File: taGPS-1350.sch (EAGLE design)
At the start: 84 parts, among them IC1 MSP430FR698X(1)80-PIN_PN, IC3 FT232RL

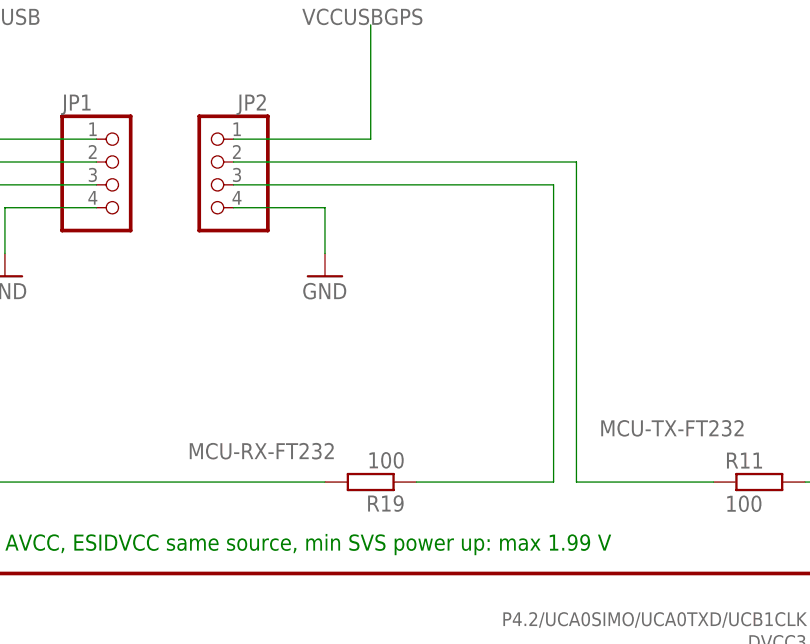
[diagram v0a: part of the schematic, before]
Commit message: Fix MCU RX/TX pinheader position, polish boards
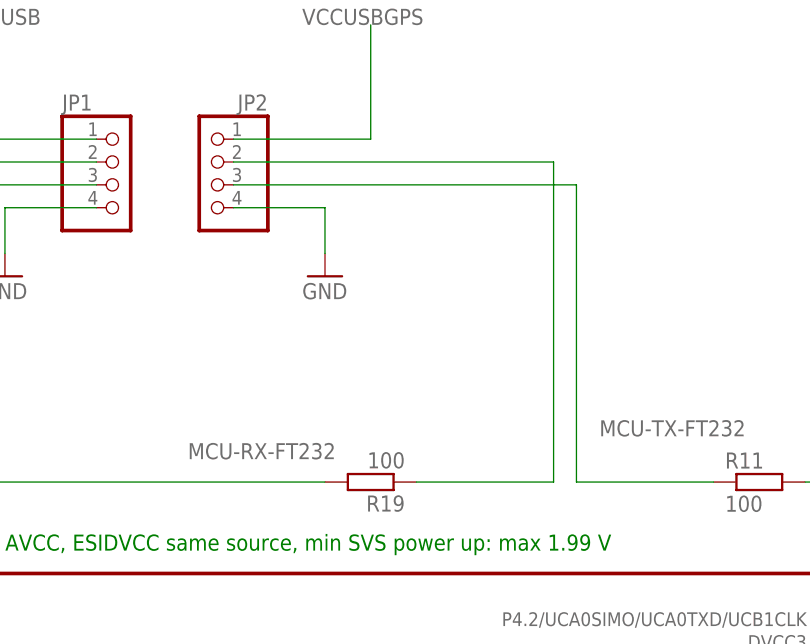
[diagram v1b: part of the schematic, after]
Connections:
- net MCU-TX-FT232: now also JP2.3; no longer JP2.2
- net N$8: now also JP2.2; no longer JP2.3
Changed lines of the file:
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@@
 <label x="-38.1" y="45.72" size="1.778" layer="95"/>
 <wire x1="-25.4" y1="40.64" x2="-40.64" y2="40.64" width="0.1524" layer="91"/>
-<wire x1="-40.64" y1="40.64" x2="-40.64" y2="76.2" width="0.1524" layer="91"/>
-<pinref part="JP2" gate="A" pin="2"/>
-<wire x1="-40.64" y1="76.2" x2="-78.74" y2="76.2" width="0.1524" layer="91"/>
+<wire x1="-40.64" y1="40.64" x2="-40.64" y2="73.66" width="0.1524" layer="91"/>
+<pinref part="JP2" gate="A" pin="3"/>
+<wire x1="-78.74" y1="73.66" x2="-40.64" y2="73.66" width="0.1524" layer="91"/>
 </segment>
 </net>
@@
 <pinref part="R19" gate="G$1" pin="1"/>
 <wire x1="-58.42" y1="40.64" x2="-43.18" y2="40.64" width="0.1524" layer="91"/>
-<wire x1="-43.18" y1="40.64" x2="-43.18" y2="73.66" width="0.1524" layer="91"/>
-<pinref part="JP2" gate="A" pin="3"/>
-<wire x1="-43.18" y1="73.66" x2="-78.74" y2="73.66" width="0.1524" layer="91"/>
-</segment>
-</net>
+<wire x1="-43.18" y1="40.64" x2="-43.18" y2="76.2" width="0.1524" layer="91"/>
+<pinref part="JP2" gate="A" pin="2"/>
+<wire x1="-43.18" y1="76.2" x2="-78.74" y2="76.2" width="0.1524" layer="91"/>
+</segment>
+</net>

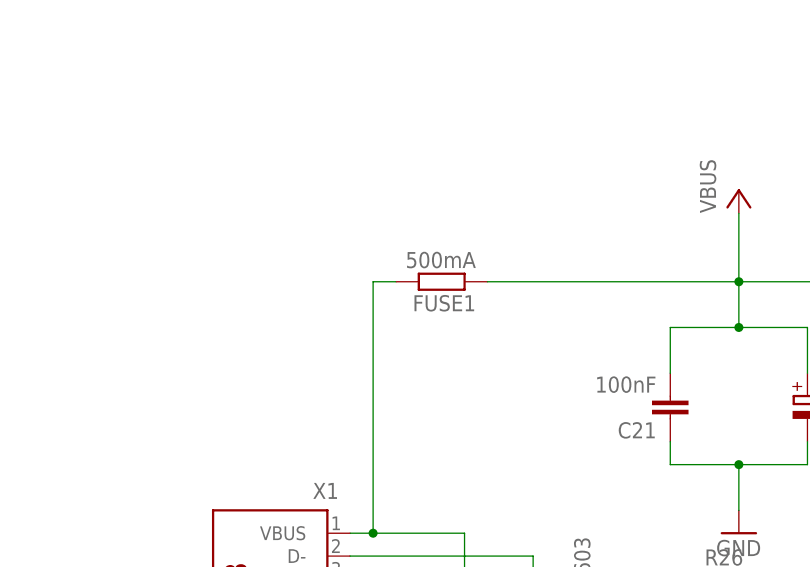
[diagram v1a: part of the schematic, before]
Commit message: Replace FUSE package to 1812
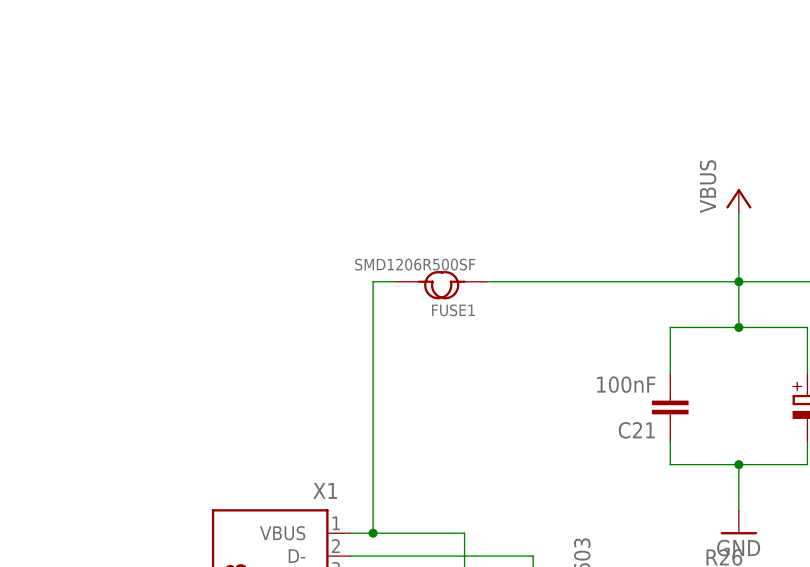
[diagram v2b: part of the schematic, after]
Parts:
- FUSE1: value 500mA -> SMD1206R500SF; device tagps:R-EU_R0805 -> tagps:SMD-PPTC-500MA-15V(1812)
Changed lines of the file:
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@@
 <layer number="48" name="Document" color="7" fill="1" visible="no" active="no"/>
 <layer number="49" name="Reference" color="7" fill="1" visible="no" active="no"/>
+<layer number="50" name="dxf" color="7" fill="1" visible="no" active="no"/>
 <layer number="51" name="tDocu" color="7" fill="1" visible="no" active="no"/>
 <layer number="52" name="bDocu" color="7" fill="1" visible="no" active="no"/>
+<layer number="53" name="tGND_GNDA" color="7" fill="9" visible="no" active="no"/>
+<layer number="54" name="bGND_GNDA" color="1" fill="9" visible="no" active="no"/>
+<layer number="56" name="wert" color="7" fill="1" visible="no" active="no"/>
+<layer number="57" name="tCAD" color="7" fill="1" visible="no" active="no"/>
 <layer number="90" name="Modules" color="5" fill="1" visible="yes" active="yes"/>
 <layer number="91" name="Nets" color="2" fill="1" visible="yes" active="yes"/>
@@
 <layer number="98" name="Guide" color="6" fill="1" visible="yes" active="yes"/>
 <layer number="99" name="SpiceOrder" color="5" fill="1" visible="yes" active="yes"/>
+<layer number="100" name="Muster" color="7" fill="1" visible="no" active="no"/>
+<layer number="101" name="Patch_Top" color="12" fill="4" visible="no" active="no"/>
+<layer number="102" name="Vscore" color="7" fill="1" visible="no" active="no"/>
+<layer number="103" name="tMap" color="7" fill="1" visible="no" active="no"/>
+<layer number="104" name="Name" color="7" fill="1" visible="no" active="no"/>
+<layer number="105" name="tPlate" color="7" fill="1" visible="no" active="no"/>
+<layer number="106" name="bPlate" color="7" fill="1" visible="no" active="no"/>
+<layer number="107" name="Crop" color="7" fill="1" visible="no" active="no"/>
+<layer number="108" name="fp8" color="7" fill="1" visible="yes" active="yes"/>
+<layer number="109" name="fp9" color="7" fill="1" visible="yes" active="yes"/>
+<layer number="110" name="110" color="7" fill="1" visible="yes" active="yes"/>
+<layer number="111" name="111" color="7" fill="1" visible="yes" active="yes"/>
+<layer number="112" name="tSilk" color="7" fill="1" visible="yes" active="yes"/>
+<layer number="113" name="IDFDebug" color="7" fill="1" visible="yes" active="yes"/>
+<layer number="114" name="FRNTMAAT1" color="7" fill="1" visible="no" active="no"/>
+<layer number="115" name="FRNTMAAT2" color="7" fill="1" visible="no" active="no"/>
+<layer number="116" name="Patch_BOT" color="9" fill="4" visible="no" active="no"/>
+<layer number="117" name="BACKMAAT1" color="7" fill="1" visible="no" active="no"/>
+<layer number="118" name="Rect_Pads" color="7" fill="1" visible="yes" active="yes"/>
+<layer number="119" name="KAP_TEKEN" color="7" fill="1" visible="no" active="no"/>
+<layer number="120" name="KAP_MAAT1" color="7" fill="1" visible="no" active="no"/>
+<layer number="121" name="_tsilk" color="7" fill="1" visible="no" active="no"/>
+<layer number="122" name="_bsilk" color="7" fill="1" visible="no" active="no"/>
+<layer number="123" name="tTestmark" color="7" fill="1" visible="yes" active="yes"/>
+<layer number="124" name="bTestmark" color="7" fill="1" visible="yes" active="yes"/>
+<layer number="125" name="_tNames" color="7" fill="1" visible="yes" active="yes"/>
+<layer number="126" name="_bNames" color="7" fill="1" visible="yes" active="yes"/>
+<layer number="127" name="_tValues" color="7" fill="1" visible="yes" active="yes"/>
+<layer number="128" name="_bValues" color="7" fill="1" visible="yes" active="yes"/>
+<layer number="130" name="SMDSTROOK" color="7" fill="1" visible="no" active="no"/>
+<layer number="131" name="tAdjust" color="7" fill="1" visible="yes" active="yes"/>
+<layer number="132" name="bAdjust" color="7" fill="1" visible="yes" active="yes"/>
+<layer number="144" name="DrillLegend" color="7" fill="1" visible="no" active="no"/>
+<layer number="150" name="Notes" color="7" fill="1" visible="yes" active="yes"/>
+<layer number="151" name="HeatSink" color="14" fill="1" visible="no" active="no"/>
+<layer number="152" name="_bDocu" color="7" fill="1" visible="yes" active="yes"/>
+<layer number="153" name="FabDoc1" color="6" fill="1" visible="no" active="no"/>
+<layer number="154" name="FabDoc2" color="2" fill="1" visible="no" active="no"/>
+<layer number="155" name="FabDoc3" color="7" fill="15" visible="no" active="no"/>
+<layer number="199" name="Contour" color="7" fill="1" visible="yes" active="yes"/>
+<layer number="200" name="200bmp" color="1" fill="10" visible="no" active="no"/>
+<layer number="201" name="201bmp" color="2" fill="1" visible="no" active="no"/>
+<layer number="202" name="202bmp" color="3" fill="1" visible="no" active="no"/>
+<layer number="203" name="203bmp" color="4" fill="10" visible="no" active="no"/>
+<layer number="204" name="204bmp" color="5" fill="10" visible="no" active="no"/>
+<layer number="205" name="205bmp" color="6" fill="10" visible="no" active="no"/>
+<layer number="206" name="206bmp" color="7" fill="10" visible="no" active="no"/>
+<layer number="207" name="207bmp" color="15" fill="10" visible="no" active="no"/>
+<layer number="208" name="208bmp" color="9" fill="10" visible="no" active="no"/>
+<layer number="209" name="209bmp" color="7" fill="1" visible="no" active="no"/>
+<layer number="210" name="210bmp" color="7" fill="1" visible="no" active="no"/>
+<layer number="211" name="211bmp" color="7" fill="1" visible="no" active="no"/>
+<layer number="212" name="212bmp" color="7" fill="1" visible="no" active="no"/>
+<layer number="213" name="213bmp" color="7" fill="1" visible="no" active="no"/>
+<layer number="214" name="214bmp" color="7" fill="1" visible="no" active="no"/>
+<layer number="215" name="215bmp" color="7" fill="1" visible="no" active="no"/>
+<layer number="216" name="216bmp" color="7" fill="1" visible="no" active="no"/>
+<layer number="217" name="217bmp" color="18" fill="1" visible="no" active="no"/>
+<layer number="218" name="218bmp" color="19" fill="1" visible="no" active="no"/>
+<layer number="219" name="219bmp" color="20" fill="1" visible="no" active="no"/>
+<layer number="220" name="220bmp" color="21" fill="1" visible="no" active="no"/>
+<layer number="221" name="221bmp" color="22" fill="1" visible="no" active="no"/>
+<layer number="222" name="222bmp" color="23" fill="1" visible="no" active="no"/>
+<layer number="223" name="223bmp" color="24" fill="1" visible="no" active="no"/>
+<layer number="224" name="224bmp" color="25" fill="1" visible="no" active="no"/>
+<layer number="225" name="225bmp" color="7" fill="1" visible="yes" active="yes"/>
+<layer number="226" name="226bmp" color="7" fill="1" visible="yes" active="yes"/>
+<layer number="227" name="227bmp" color="7" fill="1" visible="yes" active="yes"/>
+<layer number="228" name="228bmp" color="7" fill="1" visible="yes" active="yes"/>
+<layer number="230" name="230bmp" color="7" fill="1" visible="yes" active="yes"/>
+<layer number="231" name="Eagle3D_PG1" color="7" fill="1" visible="no" active="no"/>
+<layer number="232" name="Eagle3D_PG2" color="7" fill="1" visible="no" active="no"/>
+<layer number="233" name="Eagle3D_PG3" color="7" fill="1" visible="no" active="no"/>
+<layer number="248" name="Housing" color="7" fill="1" visible="yes" active="yes"/>
+<layer number="249" name="Edge" color="7" fill="1" visible="yes" active="yes"/>
+<layer number="250" name="Descript" color="3" fill="1" visible="no" active="no"/>
+<layer number="251" name="SMDround" color="12" fill="11" visible="no" active="no"/>
+<layer number="254" name="OrgLBR" color="13" fill="1" visible="no" active="no"/>
+<layer number="255" name="Accent" color="7" fill="1" visible="no" active="no"/>
 </layers>
 <schematic xreflabel="%F%N/%S.%C%R" xrefpart="/%S.%C%R">
@@
 <classes>
 <class number="0" name="signal" width="0.254" drill="0.254">
-<clearance class="0" value="0.1"/>
+<clearance class="0" value="0.15"/>
 </class>
 <class number="1" name="charimp50" width="0.254" drill="0.254">
-<clearance class="1" value="0.1"/>
+<clearance class="1" value="0.15"/>
 </class>
 <class number="2" name="conect" width="0.254" drill="0.254">
@@
 <part name="R30" library="tagps" deviceset="R-EU_" device="R0603" value="100"/>
 <part name="R31" library="tagps" deviceset="R-EU_" device="R0603" value="100"/>
-<part name="FUSE1" library="tagps" deviceset="R-EU_" device="R0805" value="500mA"/>
+<part name="FUSE1" library="tagps" deviceset="SMD-PPTC-500MA-15V(1812)" device="" value="SMD1206R500SF"/>
 <part name="VAR1" library="tagps" deviceset="VARISTOR" device="CN0603"/>
 <part name="VAR2" library="tagps" deviceset="VARISTOR" device="CN0603"/>

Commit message: Redesign type 1350 to get wider copper plane for antenna
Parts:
- TP-VCC: value TPSQPAD1-13 -> TPSQTP10R; device tagps:TPSQPAD1-13 -> tagps:TPSQTP10R
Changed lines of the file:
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@@
 <part name="C27" library="tagps" deviceset="CPOL-EU" device="A/3216-18W" value="1uF"/>
 <part name="C28" library="tagps" deviceset="CPOL-EU" device="A/3216-18W" value="4.7uF"/>
-<part name="TP-VCC" library="tagps" deviceset="TPSQ" device="PAD1-13" value="TPSQPAD1-13"/>
+<part name="TP-VCC" library="tagps" deviceset="TPSQ" device="TP10R" value="TPSQTP10R"/>
 <part name="TP-USBRX" library="tagps" deviceset="TPSQ" device="PAD1-13" value="TPSQPAD1-13"/>
 <part name="TP-USBTX" library="tagps" deviceset="TPSQ" device="PAD1-13" value="TPSQPAD1-13"/>

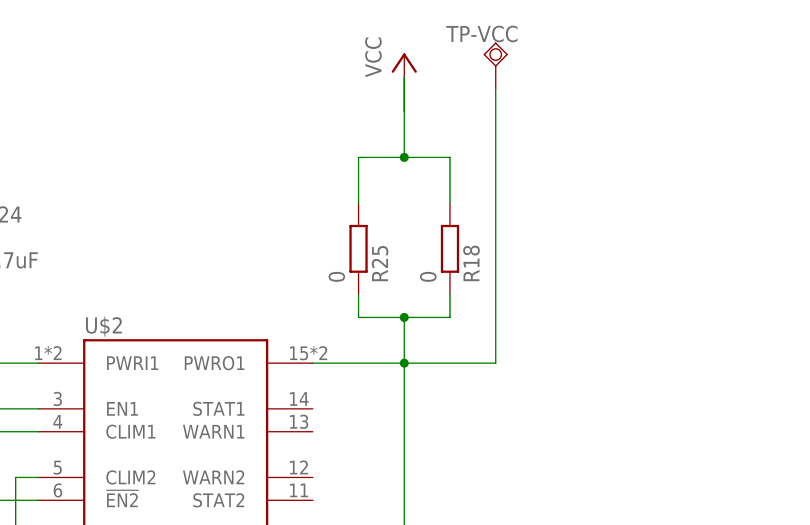
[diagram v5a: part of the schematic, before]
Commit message: Remove DC power shunts
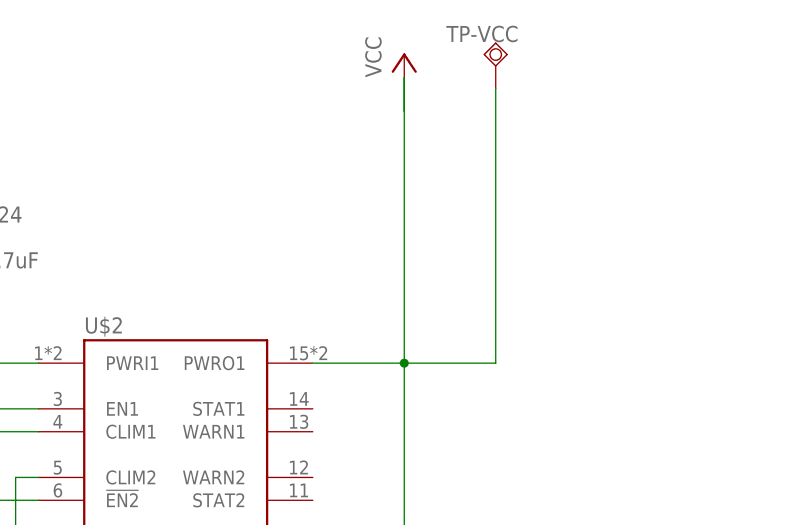
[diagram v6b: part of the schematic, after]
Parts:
- removed R18, R25: 0, tagps:R-EU_R0603
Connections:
- removed net N$26: C18.1, R18.1, R25.1, TP-VCC.TP, U$2.PWRO1, U$2.PWRO2
- net VCC: now also C18.1, TP-VCC.TP, U$2.PWRO1, U$2.PWRO2; no longer R18.2, R25.2
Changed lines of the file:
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@@
 <part name="GND37" library="supply1" deviceset="GND" device=""/>
 <part name="GND36" library="supply1" deviceset="GND" device=""/>
-<part name="R18" library="tagps" deviceset="R-EU_" device="R0603" value="0"/>
 <part name="JP1" library="tagps" deviceset="PINHD-1X4" device=""/>
 <part name="JP2" library="tagps" deviceset="PINHD-1X4" device=""/>
@@
 <part name="R20" library="tagps" deviceset="R-EU_" device="R0603" value="100"/>
 <part name="GND12" library="supply1" deviceset="GND" device=""/>
-<part name="R25" library="tagps" deviceset="R-EU_" device="R0603" value="0"/>
 <part name="R26" library="tagps" deviceset="R-EU_" device="R0603" value="0"/>
 <part name="R28" library="tagps" deviceset="R-EU_" device="R0603" value="100"/>
@@
 <instance part="GND37" gate="1" x="491.49" y="-40.64"/>
 <instance part="GND36" gate="1" x="535.94" y="-97.79"/>
-<instance part="R18" gate="G$1" x="281.94" y="210.82" rot="MR90"/>
 <instance part="JP1" gate="A" x="-91.44" y="73.66"/>
 <instance part="JP2" gate="A" x="-81.28" y="73.66" rot="MR0"/>
@@
 <instance part="R20" gate="G$1" x="-190.5" y="170.18"/>
 <instance part="GND12" gate="1" x="-104.14" y="63.5"/>
-<instance part="R25" gate="G$1" x="271.78" y="210.82" rot="MR90"/>
 <instance part="R26" gate="G$1" x="-284.48" y="139.7"/>
 <instance part="R28" gate="G$1" x="-180.34" y="-60.96" rot="R180"/>
@@
 </segment>
 <segment>
-<pinref part="R25" gate="G$1" pin="2"/>
-<wire x1="271.78" y1="215.9" x2="271.78" y2="220.98" width="0.1524" layer="91"/>
-<wire x1="271.78" y1="220.98" x2="276.86" y2="220.98" width="0.1524" layer="91"/>
-<wire x1="276.86" y1="220.98" x2="276.86" y2="229.87" width="0.1524" layer="91"/>
-<pinref part="R18" gate="G$1" pin="2"/>
 <wire x1="276.86" y1="229.87" x2="276.86" y2="226.06" width="0.1524" layer="91"/>
-<wire x1="281.94" y1="215.9" x2="281.94" y2="220.98" width="0.1524" layer="91"/>
-<wire x1="281.94" y1="220.98" x2="276.86" y2="220.98" width="0.1524" layer="91"/>
-<junction x="276.86" y="220.98"/>
 <pinref part="P+10" gate="VCC" pin="VCC"/>
+<pinref part="U$2" gate="G$1" pin="PWRO2"/>
+<wire x1="266.7" y1="177.8" x2="276.86" y2="177.8" width="0.1524" layer="91"/>
+<wire x1="276.86" y1="177.8" x2="276.86" y2="198.12" width="0.1524" layer="91"/>
+<pinref part="U$2" gate="G$1" pin="PWRO1"/>
+<wire x1="276.86" y1="198.12" x2="266.7" y2="198.12" width="0.1524" layer="91"/>
+<junction x="276.86" y="198.12"/>
+<pinref part="C18" gate="G$1" pin="1"/>
+<wire x1="276.86" y1="170.18" x2="276.86" y2="177.8" width="0.1524" layer="91"/>
+<junction x="276.86" y="177.8"/>
+<pinref part="TP-VCC" gate="G$1" pin="TP"/>
+<wire x1="287.02" y1="228.6" x2="287.02" y2="198.12" width="0.1524" layer="91"/>
+<wire x1="287.02" y1="198.12" x2="276.86" y2="198.12" width="0.1524" layer="91"/>
+<wire x1="276.86" y1="229.87" x2="276.86" y2="198.12" width="0.1524" layer="91"/>
 </segment>
 </net>
@@
 </segment>
 </net>
-<net name="N$26" class="0">
-<segment>
-<pinref part="U$2" gate="G$1" pin="PWRO2"/>
-<wire x1="266.7" y1="177.8" x2="276.86" y2="177.8" width="0.1524" layer="91"/>
-<wire x1="276.86" y1="177.8" x2="276.86" y2="198.12" width="0.1524" layer="91"/>
-<pinref part="U$2" gate="G$1" pin="PWRO1"/>
-<wire x1="276.86" y1="198.12" x2="266.7" y2="198.12" width="0.1524" layer="91"/>
-<junction x="276.86" y="198.12"/>
-<pinref part="C18" gate="G$1" pin="1"/>
-<wire x1="276.86" y1="170.18" x2="276.86" y2="177.8" width="0.1524" layer="91"/>
-<junction x="276.86" y="177.8"/>
-<pinref part="TP-VCC" gate="G$1" pin="TP"/>
-<wire x1="287.02" y1="228.6" x2="287.02" y2="198.12" width="0.1524" layer="91"/>
-<wire x1="287.02" y1="198.12" x2="276.86" y2="198.12" width="0.1524" layer="91"/>
-<wire x1="276.86" y1="198.12" x2="276.86" y2="203.2" width="0.1524" layer="91"/>
-<pinref part="R25" gate="G$1" pin="1"/>
-<wire x1="276.86" y1="203.2" x2="271.78" y2="203.2" width="0.1524" layer="91"/>
-<wire x1="271.78" y1="203.2" x2="271.78" y2="205.74" width="0.1524" layer="91"/>
-<pinref part="R18" gate="G$1" pin="1"/>
-<wire x1="281.94" y1="205.74" x2="281.94" y2="203.2" width="0.1524" layer="91"/>
-<wire x1="281.94" y1="203.2" x2="276.86" y2="203.2" width="0.1524" layer="91"/>
-<junction x="276.86" y="203.2"/>
-</segment>
-</net>

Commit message: Add Ferrite Beads for GPS chip, modify battery input
For battery input one capacitor package was modified...
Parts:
- added FB0, FB1, FB2, FB3: (no value), tagps:R-EU_R0402
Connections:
- new net N$15: FB0.2, U$6.RXD
- new net N$26: FB1.2, U$6.TXD
- new net N$49: FB2.1, U$6.TIMEPULSE
- new net N$50: FB3.1, U$6.EXTINT
- net MB-GPS-RX: now also FB0.1; no longer U$6.RXD
- net MB-GPS-TX: now also FB1.1; no longer U$6.TXD
- net N$46: now also FB3.2; no longer U$6.EXTINT
- net N$47: now also FB2.2; no longer U$6.TIMEPULSE
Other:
- moved on the sheet: C13, C14, R34, R35, U$6
